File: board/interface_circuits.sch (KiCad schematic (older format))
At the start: 53 parts, among them J1 Conn_01x03, J2 Conn_01x03, K1 EE2-12NU, K2 EE2-12NU, Q1 MMBT3904, Q2 MMBT3904, Q3 MMBT3904, U1 LMR16006XDDC

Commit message: Board: minor schematic tweaks, footprint creation, and initial subcircuit layout
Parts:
- removed RN1, RN10, RN11, RN12, RN13, RN14, RN15, RN16, RN2, RN3, RN4, RN5, RN6, RN7, RN8, RN9: 3.3k, Resistor_THT:R_Array_SIP9, symbol Device:R_Network08_US
- added RN1, RN10, RN11, RN12, RN13, RN14, RN15, RN16, RN2, RN3, RN4, RN5, RN6, RN7, RN8, RN9: 3.3k, agc_monitor:EXB-2HV332JV, symbol agc_monitor:R_Network08_Isolated
- C1, C3: footprint (none) -> Capacitor_Tantalum_SMD:CP_EIA-6032-28_Kemet-C
- C2, C4: footprint (none) -> Capacitor_SMD:C_0603_1608Metric
- D1, D2, D3: footprint (none) -> Diode_SMD:D_SOD-123
- J1, J2: footprint (none) -> Connector_PinHeader_2.54mm:PinHeader_1x03_P2.54mm_Vertical
- K1, K2: footprint (none) -> agc_monitor:Kemet-EE2
- L1: footprint (none) -> agc_monitor:SRR1210-680M
- L2: footprint (none) -> Inductor_SMD:L_1812_4532Metric
- R1, R10, R11, R12, R13, R14, R15, R16, R17, R18, R19, R2, R20, R3, R4, R5, R6, R7, R8, R9: footprint (none) -> Resistor_SMD:R_0603_1608Metric
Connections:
- net labels removed: MTHI
- wire segments 253 -> 497
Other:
- moved on the sheet: R14

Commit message: Board: minor redesign and initial ideas for layout
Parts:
- removed C3: 22uF, Capacitor_Tantalum_SMD:CP_EIA-6032-28_Kemet-C, symbol Device:CP1_Small
- removed C4: 100nF, Capacitor_SMD:C_0603_1608Metric, symbol Device:C_Small
- removed D1: 30V,500mA, Diode_SMD:D_SOD-123, symbol Device:D_Schottky_ALT
- removed D2, D3: D_ALT, Diode_SMD:D_SOD-123, symbol Device:D_ALT
- removed K1, K2: EE2-12NU, agc_monitor:Kemet-EE2, symbol agc_monitor:EE2-12NU
- removed L1: 68uH, agc_monitor:SRR1210-680M, symbol Device:L
- removed R1: 28k, Resistor_SMD:R_0603_1608Metric, symbol Device:R_US
- removed R10: 3.3k, Resistor_SMD:R_0603_1608Metric, symbol Device:R_US
- removed R11, R12, R6, R7: 0, Resistor_SMD:R_0603_1608Metric, symbol Device:R_US
- removed R2: 8.45k, Resistor_SMD:R_0603_1608Metric, symbol Device:R_US
- removed R5, R9: 150, Resistor_SMD:R_0603_1608Metric, symbol Device:R_US
- removed U1: LMR16006XDDC, Package_TO_SOT_SMD:SOT-23-6, symbol Regulator_Switching:LMR16006YQ3
- added C3: 0.1uF, Capacitor_SMD:C_0603_1608Metric, symbol Device:C_Small
- added Q2: MMBT3904, Package_TO_SOT_SMD:SOT-23, symbol Transistor_BJT:MMBT3904
- added R3: 1.5k, Resistor_SMD:R_0603_1608Metric, symbol Device:R_US
- added U1: TLV73333P_SOT23-5, Package_TO_SOT_SMD:SOT-23-5, symbol agc_monitor:TLV73333P_SOT23-5
- C1: value 6.8uF -> 12uF
- C2: value 4.7uF -> 0.1uF
- R1: renamed from R3; value 0 -> 10k
- RN1, RN10, RN11, RN12, RN13, RN14, RN15, RN16, RN2, RN3, RN4, RN5, RN6, RN7, RN8, RN9: footprint agc_monitor:EXB-2HV332JV -> Package_SO:SOIC-16W_5.3x10.2mm_P1.27mm
- renumbered L2 to L1, Q2 to Q1, Q1 to Q4, R18 to R10, R19 to R11, R20 to R12, R4 to R2, R8 to R4, R13 to R5, R14 to R6, R15 to R7, R16 to R8, R17 to R9
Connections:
- net labels added: NHSTRT1, NHSTRT2
- net labels removed: NHALGA_R, NHSTRT_R
- wire segments 497 -> 455
- no-connect marks 5 -> 2
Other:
- note added: "Inhibit Circuits"
- note removed: "DNP"
- note removed: "Inhibit Relays"
- moved on the sheet: C1, J1, L1, Q1, Q3, R1, R2, R4

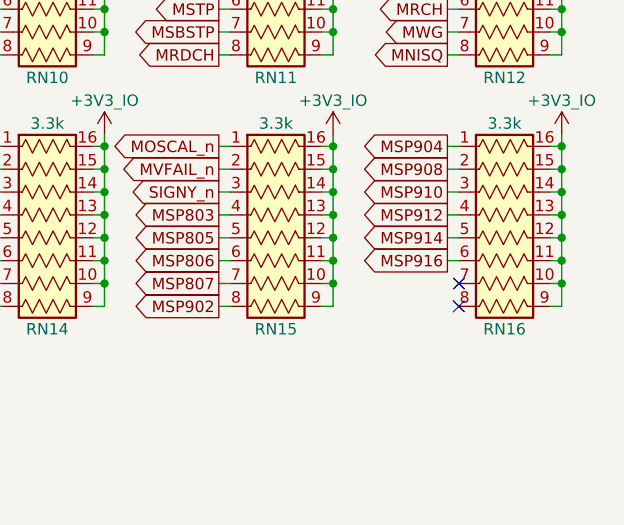
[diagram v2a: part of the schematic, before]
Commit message: Board: a bit more layout work on TC breakout
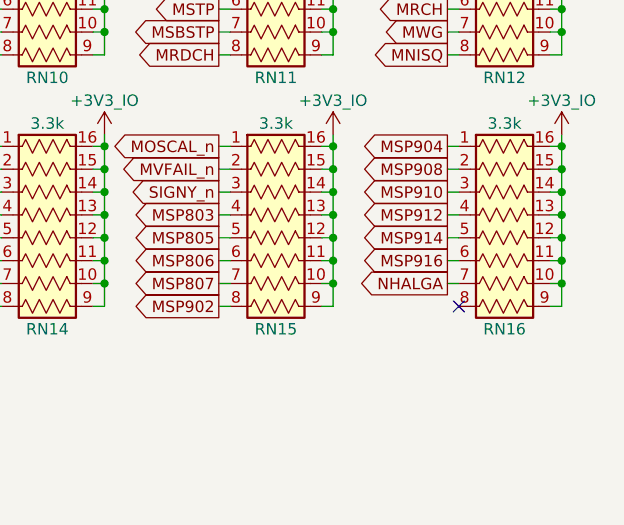
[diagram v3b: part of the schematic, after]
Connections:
- wire segments 455 -> 456
- no-connect marks 2 -> 1
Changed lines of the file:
@@
 Wire Wire Line
 	3900 3750 3950 3750
-NoConn ~ 9950 5850
 NoConn ~ 9950 5950
 Text GLabel 8900 5450 0    50   Output ~ 0
@@
 Wire Wire Line
 	2550 2050 2800 2050
+Text GLabel 9900 5850 0    50   Output ~ 0
+NHALGA
+Wire Wire Line
+	9900 5850 9950 5850
 $EndSCHEMATC

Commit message: Board: a couple more power supply changes, and completed initial TC breakout
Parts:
- removed C3: 0.1uF, Capacitor_SMD:C_0603_1608Metric, symbol Device:C_Small
- removed U1: TLV73333P_SOT23-5, Package_TO_SOT_SMD:SOT-23-5, symbol agc_monitor:TLV73333P_SOT23-5
- added C3: 10uF, Capacitor_Tantalum_SMD:CP_EIA-6032-28_Kemet-C, symbol Device:CP1_Small
- added R13: 7.5k, Resistor_SMD:R_0603_1608Metric, symbol Device:R_US
- added R14: 10k, Resistor_SMD:R_0603_1608Metric, symbol Device:R_US
- added TP1, TP2: TestPoint, TestPoint:TestPoint_Pad_D1.0mm, symbol Connector:TestPoint
- added U1: TPS77633_SO8, Package_SO:SOIC-8_3.9x4.9mm_P1.27mm, symbol agc_monitor:TPS77633_SO8
- added U2: STMPS2151_SOT23-5, Package_TO_SOT_SMD:SOT-23-5, symbol agc_monitor:STMPS2151_SOT23-5
- C1: value 12uF -> 10uF
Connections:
- net labels removed: +3V3_FPGA
- wire segments 456 -> 465
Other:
- note added: "FPGA 3.3V Switch"
- moved on the sheet: C1, C2, J1, L1, Q1, Q2, Q3, R1, R2, R3, R4

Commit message: Board: more layout work
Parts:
- J1: footprint Connector_PinHeader_2.54mm:PinHeader_1x03_P2.54mm_Vertical -> Connector_PinHeader_2.00mm:PinHeader_1x03_P2.00mm_Vertical
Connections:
- net +3V3_AGC: no longer U2.5 (IN)
- net DOSCAL: now also RN13.5 (R5A); no longer RN13.7 (R7A)
- net MAMU: now also RN10.3 (R3A); no longer RN13.6 (R6A)
- net MBR1: now also RN12.2 (R2A); no longer RN9.1 (R1A)
- net MBR2: now also RN4.5 (R5A); no longer RN9.2 (R2A)
- net MCTRAL_n: now also RN3.6 (R6A); no longer RN9.4 (R4A)
- net MDT01: now also RN4.7 (R7A); no longer RN1.1 (R1A)
- net MDT02: now also RN4.6 (R6A); no longer RN1.2 (R2A)
- net MDT03: now also RN3.8 (R8A); no longer RN1.3 (R3A)
- net MDT04: now also RN3.7 (R7A); no longer RN1.4 (R4A)
- net MDT05: now also RN2.8 (R8A); no longer RN1.5 (R5A)
- net MDT06: now also RN2.7 (R7A); no longer RN1.6 (R6A)
- net MDT07: now also RN2.1 (R1A); no longer RN1.7 (R7A)
- net MDT09: now also RN8.8 (R8A); no longer RN3.1 (R1A)
- net MDT10: now also RN8.7 (R7A); no longer RN3.2 (R2A)
- net MDT11: now also RN7.7 (R7A); no longer RN3.3 (R3A)
- net MDT12: now also RN7.6 (R6A); no longer RN3.4 (R4A)
- net MDT13: now also RN6.7 (R7A); no longer RN3.5 (R5A)
- net MDT14: now also RN6.6 (R6A); no longer RN3.6 (R6A)
- net MDT15: now also RN5.6 (R6A); no longer RN3.7 (R7A)
- net MDT16: now also RN5.5 (R5A); no longer RN3.8 (R8A)
- net MGOJAM: now also RN8.6 (R6A); no longer RN10.1 (R1A)
- net MGP_n: now also RN7.4 (R4A); no longer RN12.1 (R1A)
- net MIIP: now also RN4.1 (R1A); no longer RN9.3 (R3A)
- net MINHL: now also RN7.8 (R8A); no longer RN10.2 (R2A)
- net MINKL: now also RN7.5 (R5A); no longer RN10.3 (R3A)
- net MLDCH: now also RN8.1 (R1A); no longer RN13.1 (R1A)
- net MLOAD: now also RN15.2 (R2A); no longer RN13.4 (R4A)
- net MNHNC: now also RN3.5 (R5A); no longer RN11.2 (R2A)
- net MNHRPT: now also RN3.2 (R2A); no longer RN11.3 (R3A)
- net MNHSBF: now also RN4.2 (R2A); no longer RN11.1 (R1A)
- net MNISQ: now also RN13.4 (R4A); no longer RN12.8 (R8A)
- net MON800: now also RN16.2 (R2A); no longer RN14.3 (R3A)
- net MONPAR: now also RN10.8 (R8A); no longer RN13.2 (R2A)
- net MONWBK: now also RN9.3 (R3A); no longer RN13.3 (R3A)
- net MONWT: now also RN6.5 (R5A); no longer RN10.5 (R5A)
- net MOSCAL_n: now also RN16.1 (R1A); no longer RN15.1 (R1A)
- net MPAL_n: now also RN1.7 (R7A); no longer RN9.7 (R7A)
- net MPIPAL_n: now also RN16.5 (R5A); no longer RN14.4 (R4A)
- net MRAG: now also RN5.3 (R3A); no longer RN12.4 (R4A)
- net MRCH: now also RN10.2 (R2A); no longer RN12.6 (R6A)
- net MRDCH: now also RN8.4 (R4A); no longer RN11.8 (R8A)
- net MREAD: now also RN15.5 (R5A); no longer RN13.5 (R5A)
- net MRGG: now also RN6.3 (R3A); no longer RN10.8 (R8A)
- net MRLG: now also RN5.4 (R4A); no longer RN10.7 (R7A)
- net MRPTAL_n: now also RN2.6 (R6A); no longer RN9.6 (R6A)
- net MRSC: now also RN5.7 (R7A); no longer RN10.6 (R6A)
- net MRULOG: now also RN15.3 (R3A); no longer RN6.5 (R5A)
- net MSBSTP: now also RN1.2 (R2A); no longer RN11.7 (R7A)
- net MSCAFL_n: now also RN15.6 (R6A); no longer RN14.8 (R8A)
- net MSCDBL_n: now also RN9.4 (R4A); no longer RN14.5 (R5A)
- net MSP: now also RN7.1 (R1A); no longer RN12.2 (R2A)
- net MSP803: now also RN12.8 (R8A); no longer RN15.4 (R4A)
- net MSP805: now also RN11.6 (R6A); no longer RN15.5 (R5A)
- net MSP806: now also RN10.4 (R4A); no longer RN15.6 (R6A)
- net MSP807: now also RN10.7 (R7A); no longer RN15.7 (R7A)
- net MSP902: now also RN12.5 (R5A); no longer RN15.8 (R8A)
- net MSP904: now also RN11.3 (R3A); no longer RN16.1 (R1A)
- net MSP908: now also RN1.6 (R6A); no longer RN16.2 (R2A)
- net MSP910: now also RN8.5 (R5A); no longer RN16.3 (R3A)
- net MSP912: now also RN14.5 (R5A); no longer RN16.4 (R4A)
- net MSP914: now also RN6.4 (R4A); no longer RN16.5 (R5A)
- net MSQ10: now also RN13.6 (R6A); no longer RN8.2 (R2A)
- net MSQ11: now also RN13.7 (R7A); no longer RN8.3 (R3A)
- net MSQ12: now also RN14.7 (R7A); no longer RN8.4 (R4A)
- net MSQ13: now also RN14.8 (R8A); no longer RN8.5 (R5A)
- net MSQ14: now also RN15.7 (R7A); no longer RN8.6 (R6A)
- net MSQ16: now also RN16.8 (R8A); no longer RN8.8 (R8A)
- net MSQEXT: now also RN15.8 (R8A); no longer RN8.7 (R7A)
- net MST1: now also RN12.1 (R1A); no longer RN7.1 (R1A)
- net MST2: now also RN12.6 (R6A); no longer RN7.2 (R2A)
- net MST3: now also RN12.7 (R7A); no longer RN7.3 (R3A)
- net MSTP: now also RN1.5 (R5A); no longer RN11.6 (R6A)
- net MSTPIT_n: now also RN1.1 (R1A); no longer RN9.8 (R8A)
- net MSTRT: now also RN2.2 (R2A); no longer RN11.5 (R5A)
- net MT01: now also RN12.3 (R3A); no longer RN5.1 (R1A)
- net MT02: now also RN12.4 (R4A); no longer RN5.2 (R2A)
- net MT03: now also RN11.1 (R1A); no longer RN5.3 (R3A)
- net MT04: now also RN11.2 (R2A); no longer RN5.4 (R4A)
- net MT05: now also RN11.8 (R8A); no longer RN5.5 (R5A)
- net MT06: now also RN10.1 (R1A); no longer RN5.6 (R6A)
- net MT07: now also RN9.1 (R1A); no longer RN5.7 (R7A)
- net MT08: now also RN9.2 (R2A); no longer RN5.8 (R8A)
- net MT09: now also RN13.2 (R2A); no longer RN6.1 (R1A)
- net MT10: now also RN13.3 (R3A); no longer RN6.2 (R2A)
- net MT11: now also RN14.2 (R2A); no longer RN6.3 (R3A)
- net MT12: now also RN14.3 (R3A); no longer RN6.4 (R4A)
- net MTCAL_n: now also RN3.1 (R1A); no longer RN9.5 (R5A)
- net MTCSAI: now also RN2.5 (R5A); no longer RN11.4 (R4A)
- net MTCSA_n: now also RN11.4 (R4A); no longer RN7.4 (R4A)
- net MVFAIL_n: now also RN16.7 (R7A); no longer RN15.2 (R2A)
- net MWAG: now also RN5.8 (R8A); no longer RN12.3 (R3A)
- net MWATCH_n: now also RN14.4 (R4A); no longer RN14.2 (R2A)
- net MWBBEG: now also RN16.4 (R4A); no longer RN6.8 (R8A)
- net MWBG: now also RN9.6 (R6A); no longer RN8.1 (R1A)
- net MWCH: now also RN11.7 (R7A); no longer RN12.5 (R5A)
- net MWEBG: now also RN16.3 (R3A); no longer RN6.7 (R7A)
- net MWFBG: now also RN15.4 (R4A); no longer RN6.6 (R6A)
- net MWG: now also RN13.1 (R1A); no longer RN12.7 (R7A)
- net MWL01: now also RN4.8 (R8A); no longer RN2.1 (R1A)
- net MWL02: now also RN4.4 (R4A); no longer RN2.2 (R2A)
- net MWL03: now also RN4.3 (R3A); no longer RN2.3 (R3A)
- net MWL04: now also RN3.4 (R4A); no longer RN2.4 (R4A)
- net MWL05: now also RN3.3 (R3A); no longer RN2.5 (R5A)
- net MWL06: now also RN2.4 (R4A); no longer RN2.6 (R6A)
- net MWL07: now also RN2.3 (R3A); no longer RN2.7 (R7A)
- net MWL08: now also RN1.4 (R4A); no longer RN2.8 (R8A)
- net MWL09: now also RN1.3 (R3A); no longer RN4.1 (R1A)
- net MWL10: now also RN8.3 (R3A); no longer RN4.2 (R2A)
- net MWL11: now also RN8.2 (R2A); no longer RN4.3 (R3A)
- net MWL12: now also RN7.3 (R3A); no longer RN4.4 (R4A)
- net MWL13: now also RN7.2 (R2A); no longer RN4.5 (R5A)
- net MWL14: now also RN6.2 (R2A); no longer RN4.6 (R6A)
- net MWL15: now also RN6.1 (R1A); no longer RN4.7 (R7A)
- net MWL16: now also RN5.2 (R2A); no longer RN4.8 (R8A)
- net MWLG: now also RN6.8 (R8A); no longer RN10.4 (R4A)
- net MWQG: now also RN9.5 (R5A); no longer RN7.8 (R8A)
- net MWSG: now also RN11.5 (R5A); no longer RN7.5 (R5A)
- net MWYG: now also RN10.6 (R6A); no longer RN7.7 (R7A)
- net MWZG: now also RN10.5 (R5A); no longer RN7.6 (R6A)
- net NHALGA: now also RN9.7 (R7A); no longer RN16.7 (R7A)
- net OUTCOM: now also RN15.1 (R1A); no longer RN14.7 (R7A)
- net SIGNY_n: now also RN5.1 (R1A); no longer RN15.3 (R3A)
- new net +3V3_FPGA: U2.5 (IN)
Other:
- moved on the sheet: R13, R14

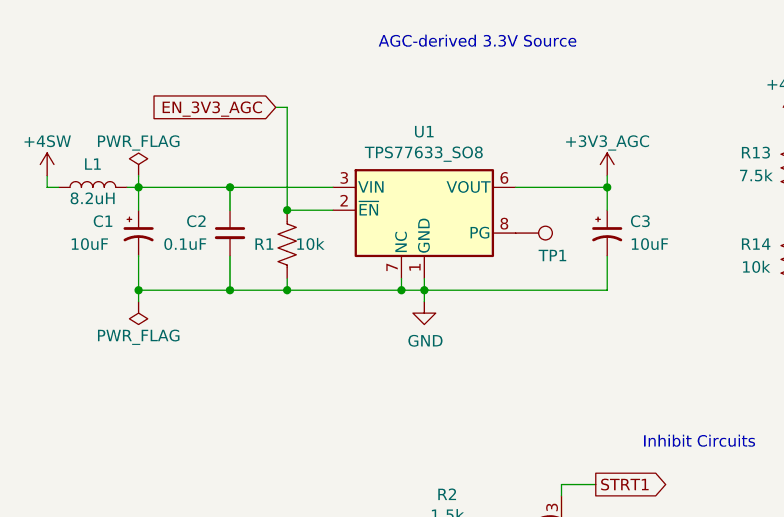
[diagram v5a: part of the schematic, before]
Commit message: Redid the mechanical outline of the board; further development/layout
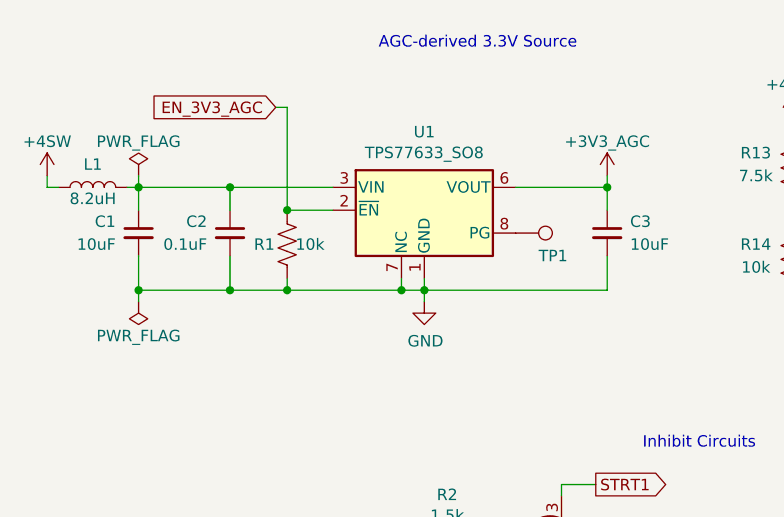
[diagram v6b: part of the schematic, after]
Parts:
- removed C1, C3: 10uF, Capacitor_Tantalum_SMD:CP_EIA-6032-28_Kemet-C, symbol Device:CP1_Small
- added C1, C3: 10uF, Capacitor_SMD:C_1206_3216Metric, symbol Device:C_Small
- J2: footprint Connector_PinHeader_2.54mm:PinHeader_1x03_P2.54mm_Vertical -> Connector_PinSocket_2.54mm:PinSocket_1x03_P2.54mm_Horizontal
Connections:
- net +3V3_AGC: now also C3.1
- net GND: now also C1.2, C3.2
- net at C2.1, L1.2, U1.3 (VIN)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: now also C1.1
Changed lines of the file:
@@
 Wire Wire Line
 	650  1750 700  1750
-$Comp
-L Device:CP1_Small C1
-U 1 1 5C73CBD2
-P 1050 1950
-F 0 "C1" H 850 2000 50  0000 L CNN
-F 1 "10uF" H 750 1900 50  0000 L CNN
-F 2 "Capacitor_Tantalum_SMD:CP_EIA-6032-28_Kemet-C" H 1050 1950 50  0001 C CNN
-F 3 "~" H 1050 1950 50  0001 C CNN
-	1    1050 1950
-	1    0    0    -1
-$EndComp
 Wire Wire Line
 	1000 1750 1050 1750
@@
 F 0 "J2" H 2079 6446 50  0000 L CNN
 F 1 "Conn_01x03" H 2080 6401 50  0001 L CNN
-F 2 "Connector_PinHeader_2.54mm:PinHeader_1x03_P2.54mm_Vertical" H 2000 6450 50  0001 C CNN
+F 2 "Connector_PinSocket_2.54mm:PinSocket_1x03_P2.54mm_Horizontal" H 2000 6450 50  0001 C CNN
 F 3 "~" H 2000 6450 50  0001 C CNN
 	1    2000 6450
@@
 $EndComp
 $Comp
-L Device:CP1_Small C3
-U 1 1 5F144E33
-P 3100 1950
-F 0 "C3" H 3200 2000 50  0000 L CNN
-F 1 "10uF" H 3200 1900 50  0000 L CNN
-F 2 "Capacitor_Tantalum_SMD:CP_EIA-6032-28_Kemet-C" H 3100 1950 50  0001 C CNN
-F 3 "~" H 3100 1950 50  0001 C CNN
-	1    3100 1950
-	1    0    0    -1
-$EndComp
-$Comp
 L agc_monitor:STMPS2151_SOT23-5 U2
 U 1 1 5F26700B
@@
 	9950 4250 9900 4250
 NoConn ~ 6950 4850
+$Comp
+L Device:C_Small C1
+U 1 1 5C92A19B
+P 1050 1950
+F 0 "C1" H 1150 2000 50  0000 L CNN
+F 1 "10uF" H 1150 1900 50  0000 L CNN
+F 2 "Capacitor_SMD:C_1206_3216Metric" H 1050 1950 50  0001 C CNN
+F 3 "~" H 1050 1950 50  0001 C CNN
+	1    1050 1950
+	-1   0    0    -1
+$EndComp
+$Comp
+L Device:C_Small C3
+U 1 1 5C967817
+P 3100 1950
+F 0 "C3" H 3200 2000 50  0000 L CNN
+F 1 "10uF" H 3200 1900 50  0000 L CNN
+F 2 "Capacitor_SMD:C_1206_3216Metric" H 3100 1950 50  0001 C CNN
+F 3 "~" H 3100 1950 50  0001 C CNN
+	1    3100 1950
+	1    0    0    -1
+$EndComp
 $EndSCHEMATC

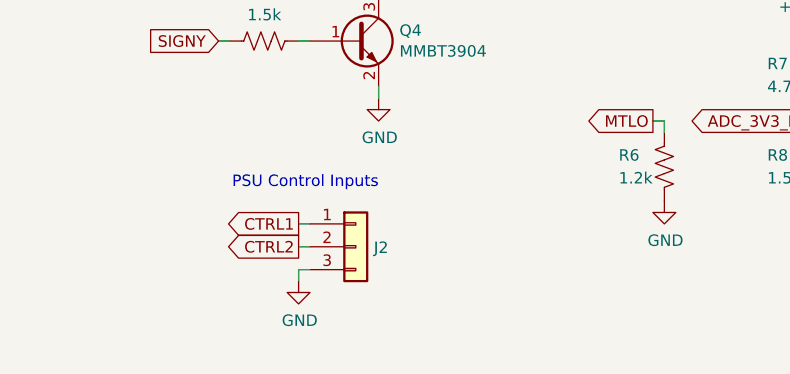
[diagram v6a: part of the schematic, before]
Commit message: Board: more rearranging work on the front; a bit more yet to come
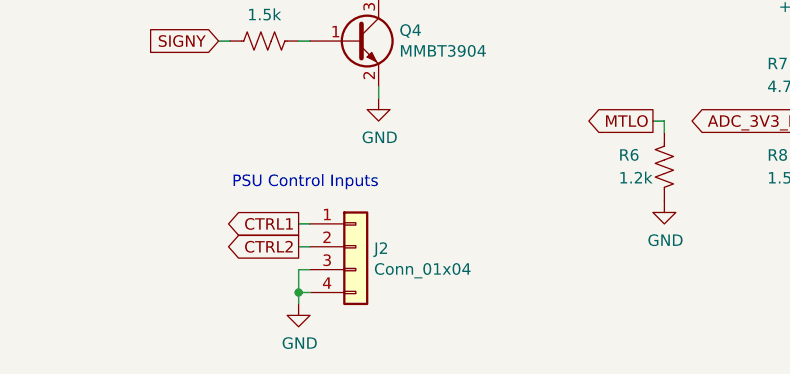
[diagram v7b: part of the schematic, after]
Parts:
- removed J2: Conn_01x03, Connector_PinSocket_2.54mm:PinSocket_1x03_P2.54mm_Horizontal, symbol Connector_Generic:Conn_01x03
- added J2: Conn_01x04, Connector_PinSocket_2.54mm:PinSocket_2x02_P2.54mm_Horizontal, symbol Connector_Generic:Conn_01x04
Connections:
- net CTRL1: now also J2.1 (Pin_1)
- net CTRL2: now also J2.2 (Pin_2)
- net GND: now also J2.3 (Pin_3), J2.4 (Pin_4)
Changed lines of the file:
@@
 L power:GND #PWR0108
 U 1 1 5C9D4435
-P 1750 6600
-F 0 "#PWR0108" H 1750 6350 50  0001 C CNN
-F 1 "GND" H 1755 6427 50  0000 C CNN
-F 2 "" H 1750 6600 50  0001 C CNN
-F 3 "" H 1750 6600 50  0001 C CNN
-	1    1750 6600
-	1    0    0    -1
-$EndComp
-Wire Wire Line
-	1750 6600 1750 6550
-Wire Wire Line
-	1800 6550 1750 6550
+P 1750 6700
+F 0 "#PWR0108" H 1750 6450 50  0001 C CNN
+F 1 "GND" H 1755 6527 50  0000 C CNN
+F 2 "" H 1750 6700 50  0001 C CNN
+F 3 "" H 1750 6700 50  0001 C CNN
+	1    1750 6700
+	1    0    0    -1
+$EndComp
+Wire Wire Line
+	1750 6700 1750 6650
+Wire Wire Line
+	1800 6650 1750 6650
 $Comp
 L agc_monitor:+3V3_AGC #PWR0109
@@
 SIGNY RTL Input
 $Comp
-L Connector_Generic:Conn_01x03 J2
-U 1 1 5EB91D30
-P 2000 6450
-F 0 "J2" H 2079 6446 50  0000 L CNN
-F 1 "Conn_01x03" H 2080 6401 50  0001 L CNN
-F 2 "Connector_PinSocket_2.54mm:PinSocket_1x03_P2.54mm_Horizontal" H 2000 6450 50  0001 C CNN
-F 3 "~" H 2000 6450 50  0001 C CNN
-	1    2000 6450
-	1    0    0    -1
-$EndComp
-$Comp
 L Connector_Generic:Conn_01x03 J1
 U 1 1 5EBA8EA1
@@
 	1    0    0    -1
 $EndComp
+$Comp
+L Connector_Generic:Conn_01x04 J2
+U 1 1 5C9F9B2F
+P 2000 6450
+F 0 "J2" H 2080 6442 50  0000 L CNN
+F 1 "Conn_01x04" H 2080 6351 50  0000 L CNN
+F 2 "Connector_PinSocket_2.54mm:PinSocket_2x02_P2.54mm_Horizontal" H 2000 6450 50  0001 C CNN
+F 3 "~" H 2000 6450 50  0001 C CNN
+	1    2000 6450
+	1    0    0    -1
+$EndComp
+Wire Wire Line
+	1750 6650 1750 6550
+Wire Wire Line
+	1750 6550 1800 6550
+Connection ~ 1750 6650
 $EndSCHEMATC

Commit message: Board: finalized v1.1 (barring any last-minute tweaks)
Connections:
- net CTRL2: now also J2.3 (Pin_3); no longer J2.2 (Pin_2)
- net GND: now also J2.2 (Pin_2); no longer J2.3 (Pin_3)
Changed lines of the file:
@@
 Wire Wire Line
 	6950 3250 6900 3250
-Text GLabel 1750 6350 0    50   Output ~ 0
+Text GLabel 1700 6350 0    50   Output ~ 0
 CTRL1
 Wire Wire Line
-	1750 6350 1800 6350
-Text GLabel 1750 6450 0    50   Output ~ 0
+	1700 6350 1800 6350
+Text GLabel 1700 6550 0    50   Output ~ 0
 CTRL2
 Wire Wire Line
-	1750 6450 1800 6450
+	1700 6550 1800 6550
 Text GLabel 3300 5900 0    50   Output ~ 0
 MTLO
@@
 $EndComp
 Wire Wire Line
-	1750 6650 1750 6550
-Wire Wire Line
-	1750 6550 1800 6550
+	1750 6650 1750 6450
 Connection ~ 1750 6650
+Wire Wire Line
+	1750 6450 1800 6450
 $EndSCHEMATC
